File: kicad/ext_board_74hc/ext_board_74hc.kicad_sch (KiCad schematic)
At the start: 26 parts, among them J1 UB13 Pin, J2 UD13 Pin, J3 UE13 Pin, J4 UB13 Socket, J5 UD13 Socket, J6 UE13 Socket, U2 74HC00

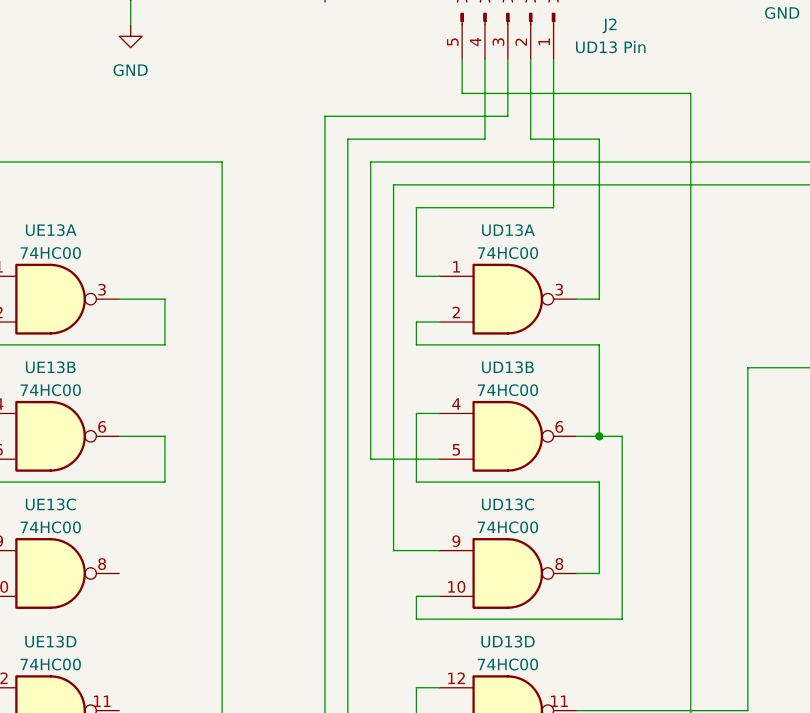
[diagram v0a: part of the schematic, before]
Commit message: Fix connections between UB-13 and UD-13
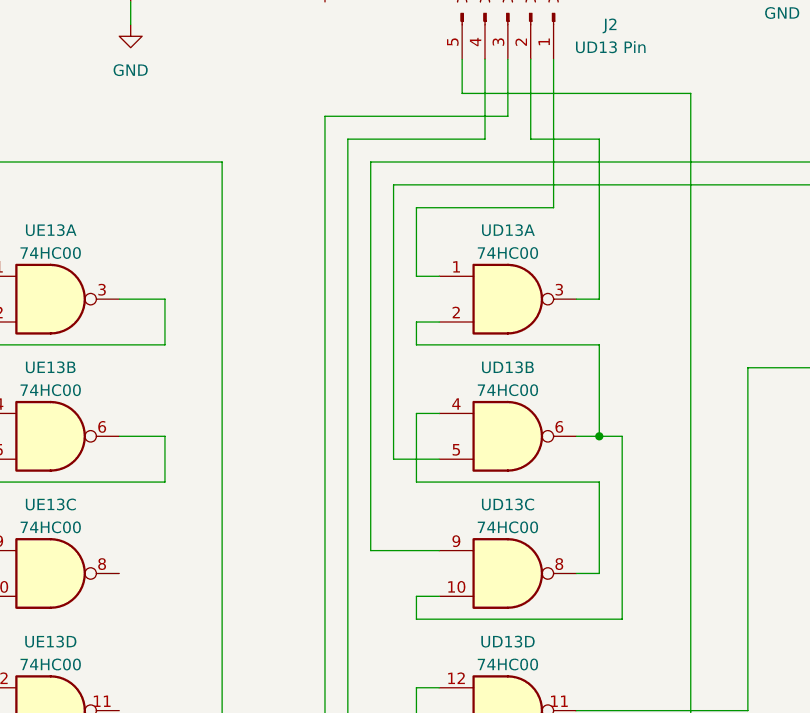
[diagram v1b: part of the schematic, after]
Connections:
- net at J1.2 (Pin_2), UB13.4 (~{S}): now also UD13.5; no longer UD13.9
- net at J1.3 (Pin_3), UB13.5 (Q): now also UD13.9; no longer UD13.5
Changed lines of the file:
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@@
-    (stroke (width 0) (type default))
-  )
-  (wire (pts (xy 167.64 113.03) (xy 175.26 113.03))
     (stroke (width 0) (type default))
   )
@@
     (stroke (width 0) (type default))
   )
+  (wire (pts (xy 167.64 80.01) (xy 167.64 123.19))
+    (stroke (width 0) (type default))
+  )
   (wire (pts (xy 144.78 100.33) (xy 116.84 100.33))
     (stroke (width 0) (type default))
@@
     (stroke (width 0) (type default))
   )
-  (wire (pts (xy 170.18 123.19) (xy 175.26 123.19))
-    (stroke (width 0) (type default))
-  )
   (wire (pts (xy 175.26 97.79) (xy 172.72 97.79))
     (stroke (width 0) (type default))
@@
     (stroke (width 0) (type default))
   )
+  (wire (pts (xy 170.18 113.03) (xy 175.26 113.03))
+    (stroke (width 0) (type default))
+  )
   (wire (pts (xy 116.84 128.27) (xy 124.46 128.27))
     (stroke (width 0) (type default))
@@
     (stroke (width 0) (type default))
   )
+  (wire (pts (xy 170.18 82.55) (xy 170.18 113.03))
+    (stroke (width 0) (type default))
+  )
   (wire (pts (xy 223.52 120.65) (xy 238.76 120.65))
     (stroke (width 0) (type default))
@@
     (stroke (width 0) (type default))
   )
-  (wire (pts (xy 170.18 82.55) (xy 170.18 123.19))
-    (stroke (width 0) (type default))
-  )
   (wire (pts (xy 86.36 118.11) (xy 82.55 118.11))
     (stroke (width 0) (type default))
@@
     (stroke (width 0) (type default))
   )
+  (wire (pts (xy 167.64 123.19) (xy 175.26 123.19))
+    (stroke (width 0) (type default))
+  )
   (wire (pts (xy 218.44 157.48) (xy 228.6 157.48))
     (stroke (width 0) (type default))
@@
     (stroke (width 0) (type default))
   )
-  (wire (pts (xy 167.64 80.01) (xy 167.64 113.03))
-    (stroke (width 0) (type default))
-  )

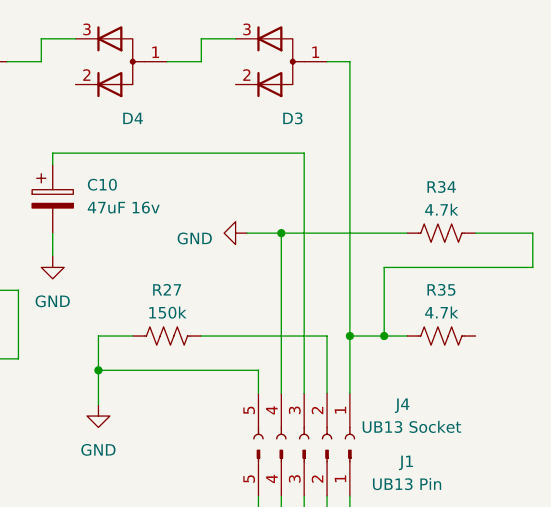
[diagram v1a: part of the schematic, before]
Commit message: Fix connection from UB-13 J1
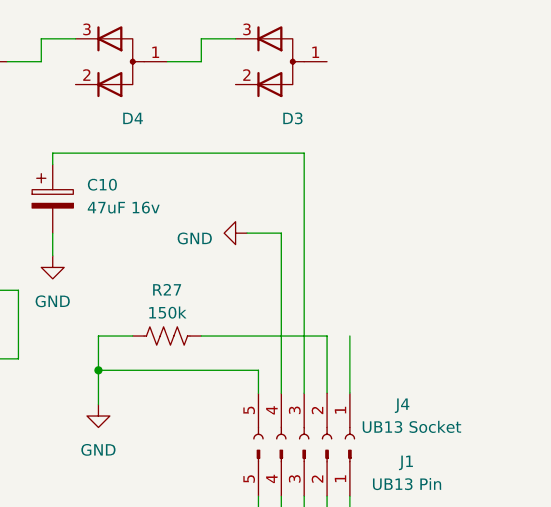
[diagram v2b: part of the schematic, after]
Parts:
- removed R34, R35: 4.7k, symbol Device:R_US
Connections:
- net at J4.1 (Pin_1): no longer D3.1 (A)
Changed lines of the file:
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@@
   (junction (at 213.36 54.61) (diameter 0) (color 0 0 0 0)
   )
-  (junction (at 233.68 39.37) (diameter 0) (color 0 0 0 0)
-  )
   (junction (at 182.88 43.18) (diameter 0) (color 0 0 0 0)
   )
@@
   (junction (at 116.84 157.48) (diameter 0) (color 0 0 0 0)
   )
-  (junction (at 241.3 50.8) (diameter 0) (color 0 0 0 0)
-  )
   (junction (at 111.76 92.71) (diameter 0) (color 0 0 0 0)
   )
@@
   (junction (at 236.22 80.01) (diameter 0) (color 0 0 0 0)
   )
-  (junction (at 245.11 50.8) (diameter 0) (color 0 0 0 0)
-  )
   (junction (at 238.76 139.7) (diameter 0) (color 0 0 0 0)
   )
@@
     (stroke (width 0) (type default))
   )
-  (wire (pts (xy 241.3 50.8) (xy 245.11 50.8))
-    (stroke (width 0) (type default))
-  )
   (wire (pts (xy 207.01 17.78) (xy 207.01 20.32))
     (stroke (width 0) (type default))
@@
     (stroke (width 0) (type default))
   )
-  (wire (pts (xy 238.76 20.32) (xy 241.3 20.32))
-    (stroke (width 0) (type default))
-  )
   (wire (pts (xy 224.79 17.78) (xy 224.79 20.32))
     (stroke (width 0) (type default))
@@
     (stroke (width 0) (type default))
   )
-  (wire (pts (xy 233.68 39.37) (xy 247.65 39.37))
-    (stroke (width 0) (type default))
-  )
   (wire (pts (xy 241.3 76.2) (xy 257.81 76.2))
     (stroke (width 0) (type default))
@@
     (stroke (width 0) (type default))
   )
-  (wire (pts (xy 261.62 39.37) (xy 261.62 43.18))
-    (stroke (width 0) (type default))
-  )
   (wire (pts (xy 195.58 130.81) (xy 172.72 130.81))
     (stroke (width 0) (type default))
@@
     (stroke (width 0) (type default))
   )
-  (wire (pts (xy 255.27 39.37) (xy 261.62 39.37))
-    (stroke (width 0) (type default))
-  )
   (wire (pts (xy 162.56 74.93) (xy 162.56 157.48))
     (stroke (width 0) (type default))
@@
     (stroke (width 0) (type default))
   )
-  (wire (pts (xy 245.11 50.8) (xy 247.65 50.8))
-    (stroke (width 0) (type default))
-  )
   (wire (pts (xy 82.55 137.16) (xy 41.91 137.16))
     (stroke (width 0) (type default))
@@
     (stroke (width 0) (type default))
   )
-  (wire (pts (xy 261.62 43.18) (xy 245.11 43.18))
-    (stroke (width 0) (type default))
-  )
   (wire (pts (xy 207.01 20.32) (xy 203.2 20.32))
     (stroke (width 0) (type default))
@@
     (stroke (width 0) (type default))
   )
-  (wire (pts (xy 241.3 20.32) (xy 241.3 50.8))
-    (stroke (width 0) (type default))
-  )
   (wire (pts (xy 114.3 97.79) (xy 124.46 97.79))
     (stroke (width 0) (type default))
@@
   )
   (wire (pts (xy 210.82 17.78) (xy 207.01 17.78))
-    (stroke (width 0) (type default))
-  )
-  (wire (pts (xy 245.11 43.18) (xy 245.11 50.8))
     (stroke (width 0) (type default))
   )
@@
     )
   )
-  (symbol (lib_id "Device:R_US") (at 251.46 50.8 90) (unit 1)
-    (in_bom yes) (on_board yes) (dnp no) (fields_autoplaced)
-    (property "Reference" "R35" (at 251.46 45.72 90)
-      (effects (font (size 1.27 1.27)))
-    )
-    (property "Value" "4.7k" (at 251.46 48.26 90)
-      (effects (font (size 1.27 1.27)))
-    )
-    (property "Footprint" "" (at 251.714 49.784 90)
-      (effects (font (size 1.27 1.27)) hide)
-    )
-    (property "Datasheet" "~" (at 251.46 50.8 0)
-      (effects (font (size 1.27 1.27)) hide)
-    )
-    (pin "1")
-    (pin "2")
-    (instances
-      (project "ext_board_74hc"
-        (path "/8fd27ab9-1fd6-4fcb-9967-31c073270cfd"
-          (reference "R35") (unit 1)
-        )
-      )
-    )
-  )
   (symbol (lib_id "74xx:74HC00") (at 182.88 95.25 0) (unit 1)
     (in_bom yes) (on_board yes) (dnp no) (fields_autoplaced)
@@
         )
       )
-    )
-  )
-  (symbol (lib_id "Device:R_US") (at 251.46 39.37 90) (unit 1)
-    (in_bom yes) (on_board yes) (dnp no) (fields_autoplaced)
-    (property "Reference" "R34" (at 251.46 34.29 90)
-      (effects (font (size 1.27 1.27)))
-    )
-    (property "Value" "4.7k" (at 251.46 36.83 90)
-      (effects (font (size 1.27 1.27)))
-    )
-    (property "Footprint" "" (at 251.714 38.354 90)
-      (effects (font (size 1.27 1.27)) hide)
-    )
-    (property "Datasheet" "~" (at 251.46 39.37 0)
-      (effects (font (size 1.27 1.27)) hide)
-    )
-    (pin "1")
-    (pin "2")
-    (instances
-      (project "ext_board_74hc"
-        (path "/8fd27ab9-1fd6-4fcb-9967-31c073270cfd"
-          (reference "R34") (unit 1)
-        )
-      )

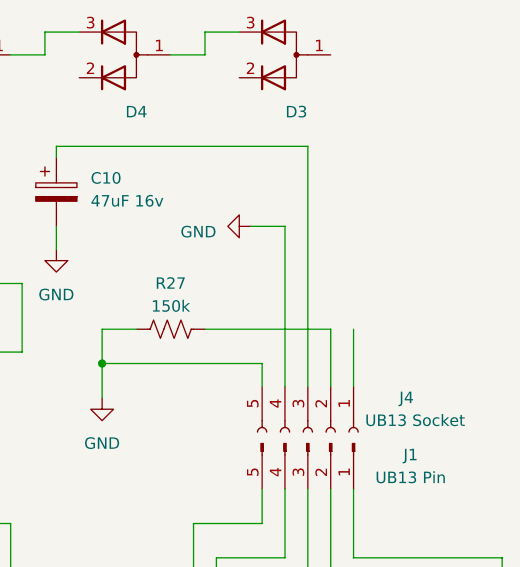
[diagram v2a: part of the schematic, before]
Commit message: Add connection UB13-1 to R112
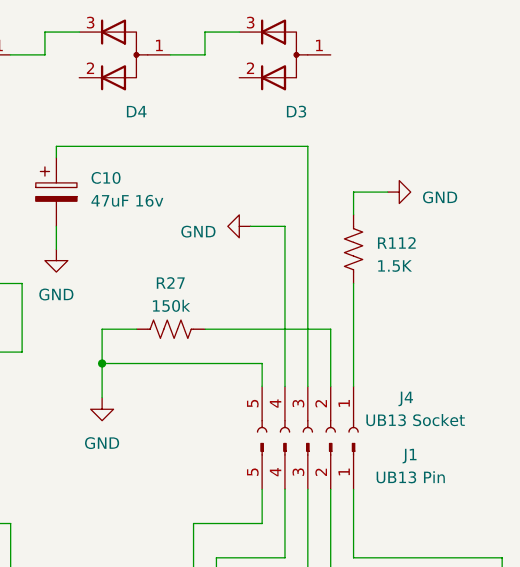
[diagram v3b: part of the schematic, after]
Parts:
- added R112: 1.5K, symbol Device:R_US
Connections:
- net GND: now also R112.1
- net at J4.1 (Pin_1): now also R112.2
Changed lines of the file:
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@@
-    (stroke (width 0) (type default))
-  )
-  (wire (pts (xy 241.3 50.8) (xy 241.3 57.15))
     (stroke (width 0) (type default))
   )
@@
     (stroke (width 0) (type default))
   )
+  (wire (pts (xy 241.3 38.1) (xy 241.3 35.56))
+    (stroke (width 0) (type default))
+  )
   (wire (pts (xy 63.5 31.75) (xy 63.5 101.6))
     (stroke (width 0) (type default))
@@
     (stroke (width 0) (type default))
   )
+  (wire (pts (xy 241.3 35.56) (xy 245.11 35.56))
+    (stroke (width 0) (type default))
+  )
   (wire (pts (xy 233.68 76.2) (xy 233.68 68.58))
     (stroke (width 0) (type default))
@@
   )
   (wire (pts (xy 203.2 72.39) (xy 203.2 157.48))
+    (stroke (width 0) (type default))
+  )
+  (wire (pts (xy 241.3 45.72) (xy 241.3 57.15))
     (stroke (width 0) (type default))
   )
@@
     )
   )
+  (symbol (lib_id "Device:R_US") (at 241.3 41.91 0) (unit 1)
+    (in_bom yes) (on_board yes) (dnp no) (fields_autoplaced)
+    (property "Reference" "R112" (at 243.84 41.275 0)
+      (effects (font (size 1.27 1.27)) (justify left))
+    )
+    (property "Value" "1.5K" (at 243.84 43.815 0)
+      (effects (font (size 1.27 1.27)) (justify left))
+    )
+    (property "Footprint" "" (at 242.316 42.164 90)
+      (effects (font (size 1.27 1.27)) hide)
+    )
+    (property "Datasheet" "~" (at 241.3 41.91 0)
+      (effects (font (size 1.27 1.27)) hide)
+    )
+    (pin "1")
+    (pin "2")
+    (instances
+      (project "ext_board_74hc"
+        (path "/8fd27ab9-1fd6-4fcb-9967-31c073270cfd"
+          (reference "R112") (unit 1)
+        )
+      )
+    )
+  )
   (symbol (lib_id "Device:C_Polarized") (at 140.97 58.42 0) (unit 1)
     (in_bom yes) (on_board yes) (dnp no) (fields_autoplaced)
@@
         )
       )
+    )
+  )
+  (symbol (lib_id "power:GND") (at 245.11 35.56 90) (unit 1)
+    (in_bom yes) (on_board yes) (dnp no) (fields_autoplaced)
+    (property "Reference" "#PWR08" (at 251.46 35.56 0)
+      (effects (font (size 1.27 1.27)) hide)
+    )
+    (property "Value" "GND" (at 248.92 36.195 90)
+      (effects (font (size 1.27 1.27)) (justify right))
+    )
+    (property "Footprint" "" (at 245.11 35.56 0)
+      (effects (font (size 1.27 1.27)) hide)
+    )
+    (property "Datasheet" "" (at 245.11 35.56 0)
+      (effects (font (size 1.27 1.27)) hide)
+    )
+    (pin "1")
+    (instances
+      (project "ext_board_74hc"
+        (path "/8fd27ab9-1fd6-4fcb-9967-31c073270cfd"
+          (reference "#PWR08") (unit 1)
+        )
+      )
